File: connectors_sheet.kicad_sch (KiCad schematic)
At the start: 4 parts, among them J1 Conn_01x04_Pin, J2 Conn_01x04_Pin, J3 Conn_01x09, J4 Conn_02x03_Counter_Clockwise

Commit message: Updated the Footprint
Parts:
- J1, J2: footprint (none) -> Connector_PinHeader_2.54mm:PinHeader_1x04_P2.54mm_Vertical
- J3: footprint (none) -> Connector_PinHeader_2.54mm:PinHeader_1x09_P2.54mm_Vertical
- J4: footprint (none) -> Connector_PinHeader_2.54mm:PinHeader_2x03_P2.54mm_Vertical
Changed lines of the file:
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@@
 			)
 		)
-		(property "Footprint" ""
+		(property "Footprint" "Connector_PinHeader_2.54mm:PinHeader_1x04_P2.54mm_Vertical"
 			(at 66.04 53.34 0)
 			(effects
@@
 			)
 		)
-		(property "Footprint" ""
+		(property "Footprint" "Connector_PinHeader_2.54mm:PinHeader_2x03_P2.54mm_Vertical"
 			(at 92.71 90.17 0)
 			(effects
@@
 			)
 		)
-		(property "Footprint" ""
+		(property "Footprint" "Connector_PinHeader_2.54mm:PinHeader_1x09_P2.54mm_Vertical"
 			(at 68.58 88.9 0)
 			(effects
@@
 			)
 		)
-		(property "Footprint" ""
+		(property "Footprint" "Connector_PinHeader_2.54mm:PinHeader_1x04_P2.54mm_Vertical"
 			(at 86.36 53.34 0)
 			(effects

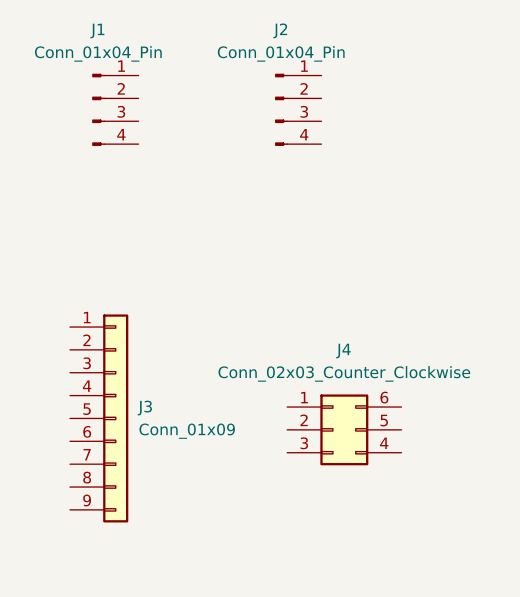
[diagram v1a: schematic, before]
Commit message: Added Pin diagram to the Connector
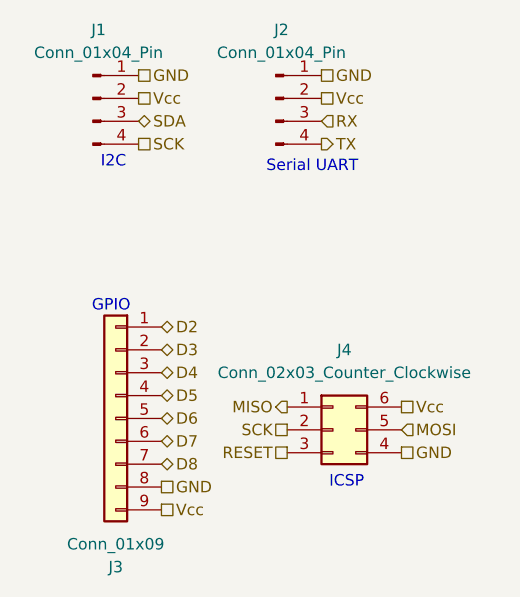
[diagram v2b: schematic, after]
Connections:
- net GND: now reaches J1.1 (Pin_1)
- net GND: now also J2.1 (Pin_1), J3.8 (Pin_8), J4.4 (Pin_4)
- net Vcc: now reaches J1.2 (Pin_2)
- net Vcc: now also J2.2 (Pin_2), J3.9 (Pin_9), J4.6 (Pin_6)
- net SDA: now reaches J1.3 (Pin_3)
- net SCK: now reaches J1.4 (Pin_4)
- net SCK: now also J4.2 (Pin_2)
- net MISO: now reaches J4.1 (Pin_1)
- net RESET: now reaches J4.3 (Pin_3)
- net MOSI: now reaches J4.5 (Pin_5)
- net D2: now reaches J3.1 (Pin_1)
- net D3: now reaches J3.2 (Pin_2)
- net D4: now reaches J3.3 (Pin_3)
- net D5: now reaches J3.4 (Pin_4)
- net D6: now reaches J3.5 (Pin_5)
- net D7: now reaches J3.6 (Pin_6)
- net D8: now reaches J3.7 (Pin_7)
- net RX: now reaches J2.3 (Pin_3)
- net TX: now reaches J2.4 (Pin_4)
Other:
- note added: "GPIO"
- note added: "I2C"
- note added: "ICSP"
- note added: "Serial UART"
- moved on the sheet: J3
